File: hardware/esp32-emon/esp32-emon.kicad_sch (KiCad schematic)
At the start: 11 parts, among them J1 SJ-3523-SMT-TR, J2 SJ-3523-SMT-TR, U1 ESP32-DEVKIT-V1

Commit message: Updates for v0.1
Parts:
- removed J2: SJ-3523-SMT-TR, Connector_Audio:Jack_3.5mm_CUI_SJ-3523-SMT_Horizontal, symbol Connector:AudioJack3
- added J2: Barrel_Jack, Connector_BarrelJack:BarrelJack_Horizontal, symbol Connector:Barrel_Jack_Switch
- added R7: 470K, Resistor_THT:R_Axial_DIN0204_L3.6mm_D1.6mm_P7.62mm_Horizontal, symbol Device:R_Small
- added TP1: VIN, TestPoint:TestPoint_THTPad_2.0x2.0mm_Drill1.0mm, symbol Connector:TestPoint
- C1, C2: footprint Capacitor_SMD:C_0603_1608Metric -> Capacitor_THT:CP_Radial_D5.0mm_P2.00mm
- R4: value 18R -> 100K
- R5: value 470K -> 1K
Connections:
- net +3V3: now also U1.1 (3V3), R7.1; no longer R5.1
- net GND: now also R6.1, U1.2 (GND), U1.29 (GND); no longer R6.2
- net ADC1 CH5: now reaches R4.1, R5.2
- net ADC1 CH5: now also U1.22 (D33); no longer C2.2, R6.1
- net at U1.30 (VIN): now also TP1.1
- net ADC1 CH7: no longer names the net of R4.2
- net ADC1 CH7: now also J2.1; no longer U1.20 (D35)
- new net: C2.2, J2.2, J2.3, R5.1, R6.2, R7.2
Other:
- note added: "AC voltage measurement"
- note added: "CT measurement"
- note added: "Reference"
- note removed: "CT 2"
- moved on the sheet: C1, J1, R1, R2, R3

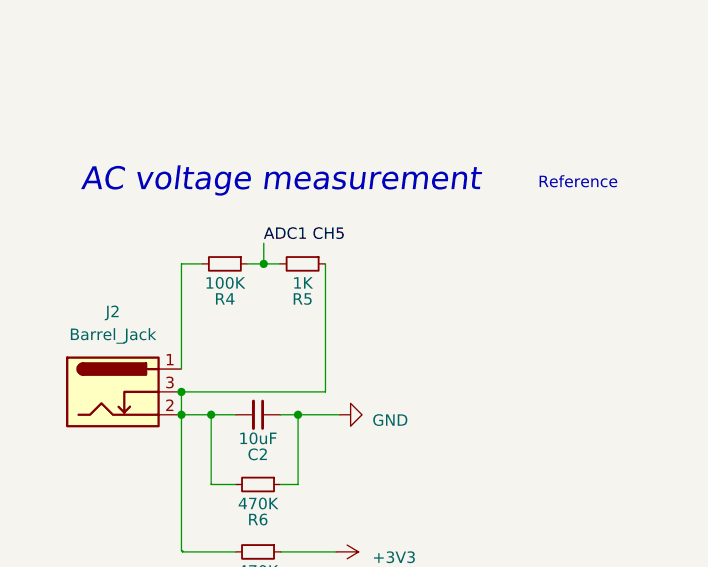
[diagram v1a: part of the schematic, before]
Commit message: Update from 1K to 10K
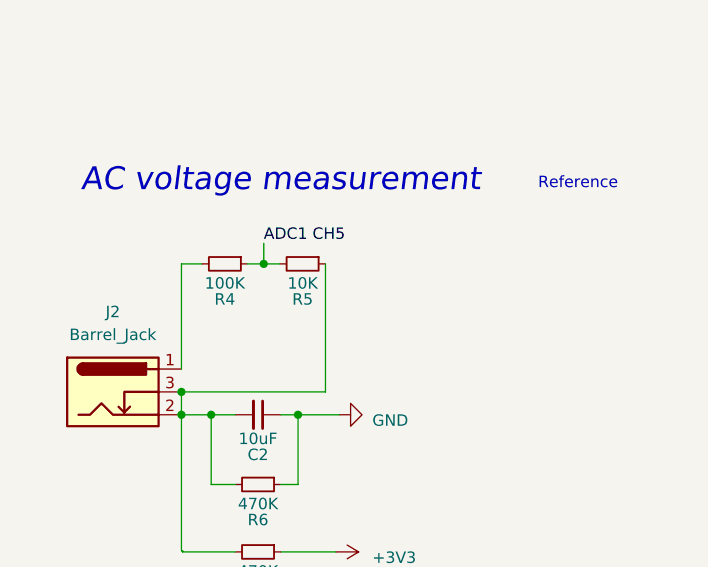
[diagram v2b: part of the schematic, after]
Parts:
- R5: value 1K -> 10K
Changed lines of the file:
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@@
       (effects (font (size 1.27 1.27)))
     )
-    (property "Value" "1K" (at 47.117 94.869 90)
+    (property "Value" "10K" (at 47.117 94.869 90)
       (effects (font (size 1.27 1.27)))
     )
